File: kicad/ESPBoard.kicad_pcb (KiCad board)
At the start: 2 copper layers, 34.3 x 59.7 mm, 23 parts, among them P1 PWR, P2 RS232, P3 GPIO, P4 3.3V, P5 Gnd, SW1 RESET, SW2 FLASH, U1 LM1117-3.3, U2 ESP-12E

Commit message: Updated board and produced Gerbers
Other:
- board text added: "FLASH"
- board text added: "RESET"
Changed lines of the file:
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@@
     (area 153.594999 90.07 188.035001 150.049762)
     (thickness 1.6)
-    (drawings 12)
+    (drawings 14)
     (tracks 180)
     (zones 0)
@@
     (visible_elements FFFFFF7F)
     (pcbplotparams
-      (layerselection 0x00030_80000001)
-      (usegerberextensions false)
+      (layerselection 0x210f0_80000001)
+      (usegerberextensions true)
       (excludeedgelayer true)
       (linewidth 0.100000)
@@
       (outputformat 1)
       (mirror false)
-      (drillshape 1)
+      (drillshape 0)
       (scaleselection 1)
       (outputdirectory ""))
@@
       (effects (font (size 1 1) (thickness 0.15)))
     )
-    (fp_text value RS232 (at 0 -3.1 90) (layer F.Fab)
+    (fp_text value RS232 (at 0 -3.1 90) (layer F.SilkS)
       (effects (font (size 1 1) (thickness 0.15)))
     )
@@
       (effects (font (size 1 1) (thickness 0.15)))
     )
-    (fp_text value GPIO (at 1.27 -2.54 270) (layer F.Fab)
+    (fp_text value GPIO (at 1.27 -2.54 90) (layer F.SilkS)
       (effects (font (size 1 1) (thickness 0.15)))
     )
@@
       (effects (font (size 1 1) (thickness 0.15)))
     )
-    (fp_text value 3.3V (at -1.27 -2.54 270) (layer F.Fab)
+    (fp_text value 3.3V (at -1.27 -2.54 90) (layer F.SilkS)
       (effects (font (size 1 1) (thickness 0.15)))
     )
@@
       (effects (font (size 1 1) (thickness 0.15)))
     )
-    (fp_text value Gnd (at 0 -2.54 270) (layer F.Fab)
+    (fp_text value Gnd (at 0 -2.54 90) (layer F.SilkS)
       (effects (font (size 1 1) (thickness 0.15)))
     )
@@
       (effects (font (size 1 1) (thickness 0.15)))
     )
-    (fp_text value RESET (at 6.35 0 90) (layer F.Fab)
+    (fp_text value RESET (at 0 0 90) (layer F.Fab)
       (effects (font (size 1 1) (thickness 0.15)))
     )
@@
       (effects (font (size 1 1) (thickness 0.15)))
     )
-    (fp_text value FLASH (at -6.35 0 270) (layer F.Fab)
+    (fp_text value FLASH (at 0 0 270) (layer F.Fab)
       (effects (font (size 1 1) (thickness 0.15)))
     )
@@
     )
   )
+  (gr_text FLASH (at 186.69 129.54 90) (layer F.SilkS)
+    (effects (font (size 1 1) (thickness 0.15)))
+  )
+  (gr_text RESET (at 186.69 135.89 90) (layer F.SilkS)
+    (effects (font (size 1 1) (thickness 0.15)))
+  )
   (gr_text A (at 175.26 91.44 90) (layer F.SilkS)

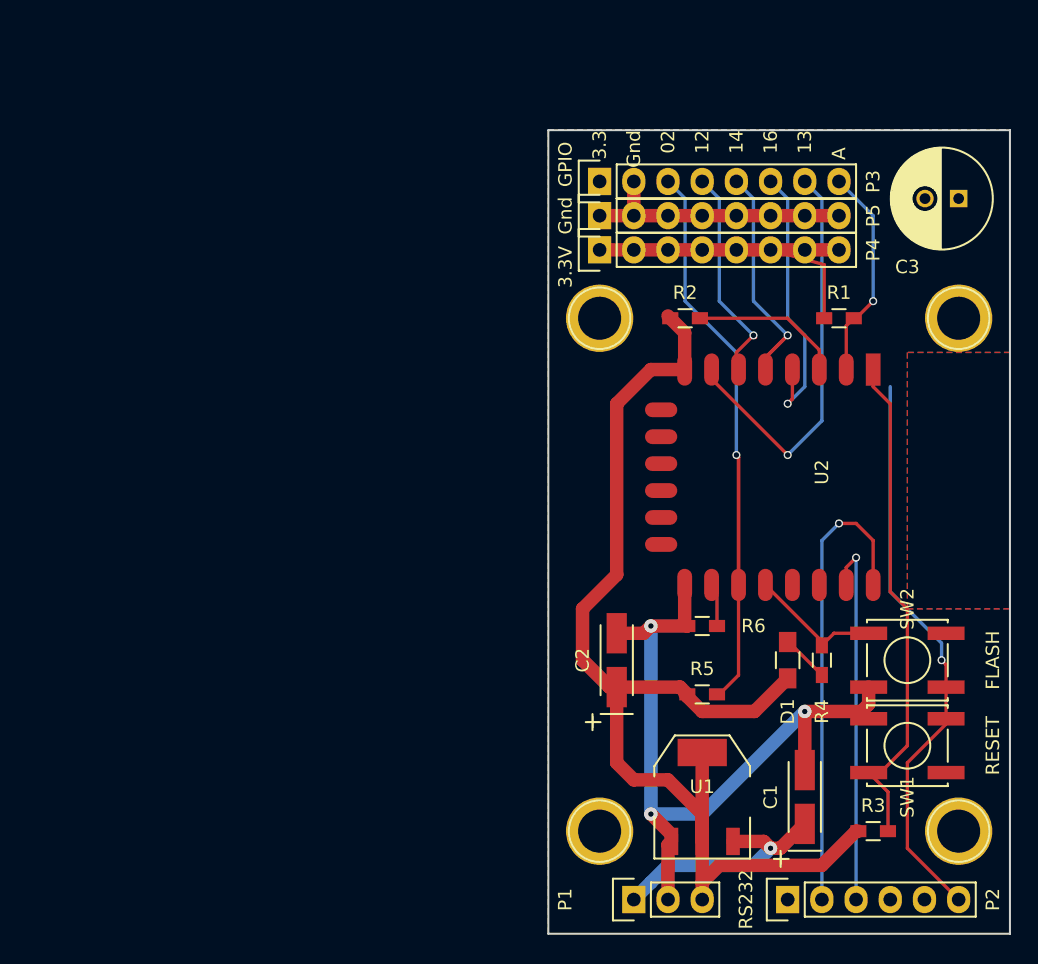
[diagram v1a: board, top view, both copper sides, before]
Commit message: Updated schematic and laid out PCB components so max dimension is less than 50mm.  Tracks still need to be connected
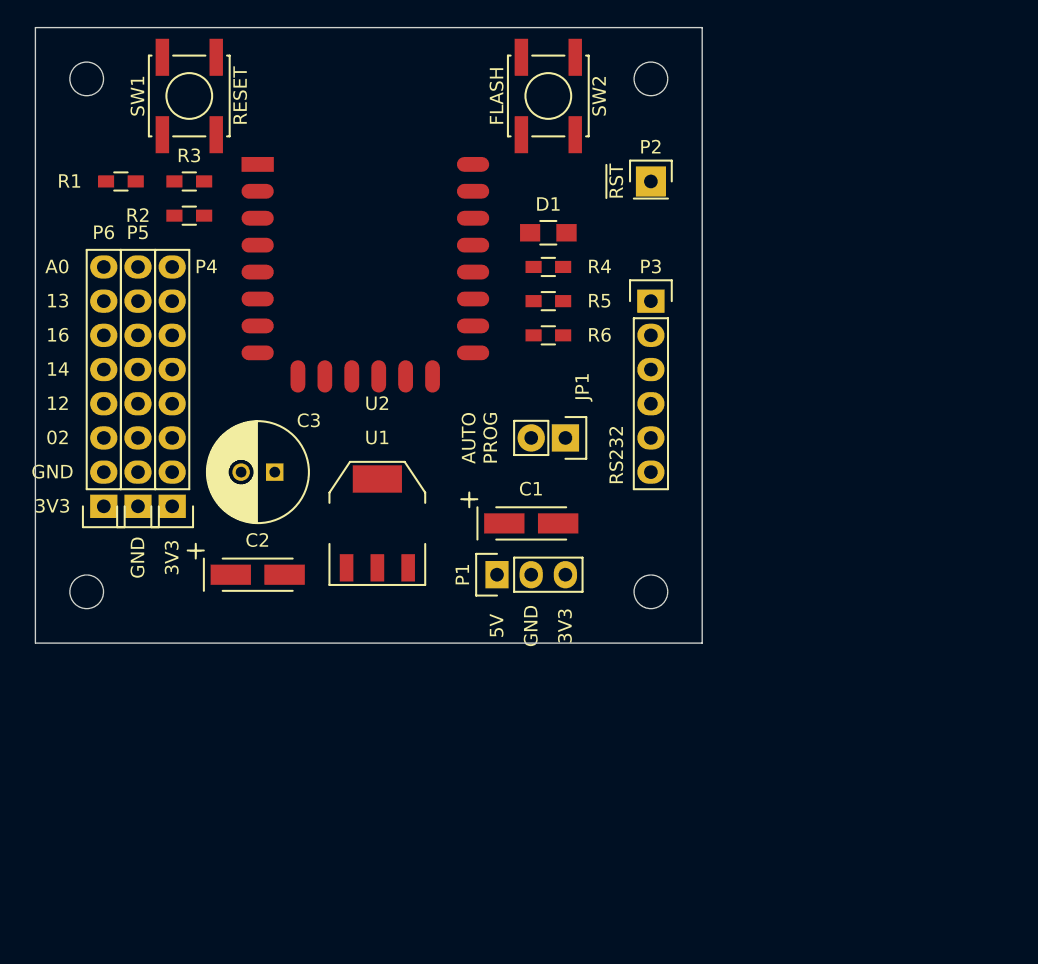
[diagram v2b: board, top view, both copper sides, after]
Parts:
- removed the REF** at (184.2, 104.1)
- removed the REF** at (157.5, 104.1)
- removed the REF** at (184.2, 142.2)
- removed the REF** at (157.5, 142.2)
- added JP1: AUTO_FLASH, Pin_Headers:Pin_Header_Straight_1x02, F.Cu at (154.9, 113.0)
- added P6: GPIO, Pin_Headers:Pin_Header_Straight_1x08, F.Cu at (120.7, 118.1)
- added REF**: MountingHole_2-5mm, Mounting_Holes:MountingHole_2-5mm, F.Cu at (119.4, 124.5)
- added REF**: MountingHole_2-5mm, Mounting_Holes:MountingHole_2-5mm, F.Cu at (119.4, 86.4)
- added REF**: MountingHole_2-5mm, Mounting_Holes:MountingHole_2-5mm, F.Cu at (161.3, 124.5)
- added REF**: MountingHole_2-5mm, Mounting_Holes:MountingHole_2-5mm, F.Cu at (161.3, 86.4)
- P2: value RS232 -> EXT_RESET; footprint Pin_Headers:Pin_Header_Straight_1x06 -> Pin_Headers:Pin_Header_Straight_1x01
- P3: value GPIO -> RS232; footprint Pin_Headers:Pin_Header_Straight_1x08 -> Pin_Headers:Pin_Header_Straight_1x06
- moved SW1 71.9 mm to (127.0, 87.6), turned to 90 degrees
- moved R3 70.1 mm to (127.0, 94.0)
- moved C3 54.7 mm to (133.3, 115.6)
- moved P2 54.3 mm to (161.3, 94.0), turned to 0 degrees
- moved R1 54.3 mm to (121.9, 94.0), turned to 180 degrees
- moved SW2 49.7 mm to (153.7, 87.6), turned to 270 degrees
- moved U2 48.2 mm to (132.1, 92.7), turned to 0 degrees
- moved P5 40.5 mm to (123.2, 118.1), turned to 180 degrees
- moved R2 37.6 mm to (127.0, 96.5)
- moved P4 37.0 mm to (125.7, 118.1), turned to 180 degrees
- moved D1 36.4 mm to (153.7, 97.8), turned to 0 degrees
- moved R4 35.6 mm to (153.7, 100.3), turned to 180 degrees
- moved U1 31.5 mm to (141.0, 119.4)
- moved R5 31.4 mm to (153.7, 102.9), turned to 180 degrees
- moved C1 28.7 mm to (152.4, 119.4), turned to 0 degrees
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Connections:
- P2 pad 1: Net-(P2-Pad1) -> /ESP_RESET
- P3 pad 1: +3V3 -> /SERIAL_DTR
- P3 pad 2: GNDPWR -> /ESP_TX_OUT
- P3 pad 3: /ESP_GPIO2 -> /ESP_RX_IN
- P3 pad 4: /ESP_GPIO12 -> /SERIAL_3V3
- P3 pad 5: /ESP_GPIO14 -> /SERIAL_CTS
- P3 pad 6: /ESP_GPIO16 -> GNDPWR
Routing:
- net +3V3: track 160.7 -> 0.00 mm
- net GNDPWR: track 133.3 -> 0.00 mm, vias 4 -> 0
- net /ESP_GPIO2: track 50.7 -> 0.00 mm, vias 1 -> 0
- net /ESP_RESET: track 37.6 -> 0.00 mm
- net /ESP_TX_OUT: track 34.8 -> 0.00 mm, vias 1 -> 0
- net /ESP_GPIO13: track 30.6 -> 0.00 mm, vias 1 -> 0
- net /ESP_RX_IN: track 27.7 -> 0.00 mm, vias 1 -> 0
- net /ESP_GPIO16: track 20.8 -> 0.00 mm, vias 1 -> 0
- net /ESP_GPIO14: track 18.6 -> 0.00 mm, vias 1 -> 0
- net +5V: track 18.0 -> 0.00 mm, vias 1 -> 0
- net /ESP_GPIO12: track 16.4 -> 0.00 mm, vias 1 -> 0
- net /ESP_ADC: track 16.0 -> 0.00 mm, vias 1 -> 0
- net /ESP_CH_PD: track 11.3 -> 0.00 mm
- net /ESP_GPIO0: track 10.1 -> 0.00 mm
- net Net-(D1-Pad1): track 3.55 -> 0.00 mm
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- removed copper zone on F.Cu, net +3V3
- removed copper zone on B.Cu, net GNDPWR
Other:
- board size 34.3 x 59.7 mm -> 49.5 x 45.7 mm
- net class Default: clearance 0.25 -> 0.2
- net class Power removed
- net class Power Small removed
- rule pad_to_mask_clearance: 0.2 -> 0
- rule trace_clearance: 0.25 -> 0.2
- rule trace_min: 0.25 -> 0.2
- board text added: "3V3"
- board text added: "5V"
- board text added: "A0"
- board text added: "AUTO PROG"
- board text added: "GND"
- board text added: "RS232"
- board text added: "~RST"
- board text removed: "3.3"
- board text removed: "A"
- board text removed: "Gnd"

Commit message: Routed the board
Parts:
- moved JP1 19.0 mm to (154.9, 94.0)
- moved R5 3.59 mm to (156.2, 105.4), turned to 270 degrees
- moved C3 2.54 mm to (130.8, 115.6), turned to 0 degrees
- moved R6 1.27 mm to (152.4, 105.4), turned to 270 degrees
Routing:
- net GNDPWR: track 0.00 -> 122.5 mm, vias 0 -> 3
- net +3V3: track 0.00 -> 83.9 mm
- net /ESP_RESET: track 0.00 -> 43.0 mm, vias 0 -> 1
- net /ESP_GPIO2: track 0.00 -> 42.4 mm
- net /ESP_GPIO13: track 0.00 -> 36.1 mm, vias 0 -> 2
- net /ESP_RX_IN: track 0.00 -> 30.4 mm, vias 0 -> 1
- net /ESP_TX_OUT: track 0.00 -> 25.1 mm, vias 0 -> 1
- net /ESP_ADC: track 0.00 -> 24.7 mm, vias 0 -> 2
- net /ESP_GPIO0: track 0.00 -> 20.2 mm
- net /ESP_GPIO12: track 0.00 -> 16.9 mm
- net /ESP_GPIO14: track 0.00 -> 15.2 mm
- net /ESP_GPIO16: track 0.00 -> 14.9 mm
- net /SERIAL_DTR: track 0.00 -> 11.5 mm
- net +5V: track 0.00 -> 10.8 mm
- net /ESP_GPIO15: track 0.00 -> 5.48 mm
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- added copper zone on F.Cu, net +3V3
- added copper zone on B.Cu, net GNDPWR
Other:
- net class Default: clearance 0.2 -> 0.25
- net class Power added: clearance 0.25, trace_width 1, via_dia 1, via_drill 0.8
- rule trace_clearance: 0.2 -> 0.25

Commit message: PCB Sent for manufacture
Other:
- board text added: "ESP Board V1.0"
- board text added: "v@nce.me"
- board text removed: "AUTO PROG"
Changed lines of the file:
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@@
     (links 63)
     (no_connects 4)
-    (area 110.844536 69.54 176.91 129.08418)
+    (area 110.844536 69.54 183.26 129.08418)
     (thickness 1.6)
-    (drawings 26)
+    (drawings 27)
     (tracks 156)
     (zones 0)
@@
     (34 B.Paste user hide)
     (35 F.Paste user hide)
-    (36 B.SilkS user hide)
+    (36 B.SilkS user)
     (37 F.SilkS user)
-    (38 B.Mask user hide)
-    (39 F.Mask user hide)
+    (38 B.Mask user)
+    (39 F.Mask user)
     (40 Dwgs.User user hide)
     (41 Cmts.User user hide)
@@
     (visible_elements FFFEFF7F)
     (pcbplotparams
-      (layerselection 0x00030_80000001)
-      (usegerberextensions false)
+      (layerselection 0x010f0_80000001)
+      (usegerberextensions true)
       (excludeedgelayer true)
       (linewidth 0.100000)
@@
       (outputformat 1)
       (mirror false)
-      (drillshape 1)
+      (drillshape 0)
       (scaleselection 1)
       (outputdirectory ""))
@@
     (descr "Through hole pin header")
     (tags "pin header")
-    (fp_text reference JP1 (at -3.81 -1.27 270) (layer F.SilkS)
+    (fp_text reference JP1 (at 0 -2.54 270) (layer F.SilkS)
       (effects (font (size 1 1) (thickness 0.15)))
     )
@@
     (descr "Through hole pin header")
     (tags "pin header")
-    (fp_text reference P2 (at 0 -2.54) (layer F.SilkS)
+    (fp_text reference P2 (at 0 2.54) (layer F.SilkS)
       (effects (font (size 1 1) (thickness 0.15)))
     )
@@
     (pad 1 thru_hole circle (at 0 0) (size 2.5 2.5) (drill 2.5) (layers))
   )
+  (gr_text "ESP Board V1.0" (at 130.81 125.73) (layer F.SilkS)
+    (effects (font (size 1.5 1.5) (thickness 0.3)))
+  )
+  (gr_text "v@nce.me\n" (at 140.97 87.63) (layer B.SilkS)
+    (effects (font (size 3 3) (thickness 0.5)) (justify mirror))
+  )
   (dimension 45.72 (width 0.3) (layer Dwgs.User)
     (gr_text "45.720 mm" (at 176.61 105.41 90) (layer Dwgs.User)
@@
     (effects (font (size 1 1) (thickness 0.15)))
   )
-  (gr_text "AUTO\nPROG" (at 148.59 113.03 90) (layer F.SilkS)
+  (gr_text ~RST (at 161.29 90.17 90) (layer F.SilkS)
     (effects (font (size 1 1) (thickness 0.15)))
   )
-  (gr_text ~RST (at 158.75 93.98 90) (layer F.SilkS)
-    (effects (font (size 1 1) (thickness 0.15)))
-  )
